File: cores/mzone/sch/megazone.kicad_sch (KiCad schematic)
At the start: 22 parts

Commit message: mzone core
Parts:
- removed B_DE9: 74LS32, symbol jt74:74LS32
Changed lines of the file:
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@@
 	(wire
 		(pts
-			(xy 68.58 135.89) (xy 76.2 135.89)
-		)
-		(stroke
-			(width 0)
-			(type default)
-		)
-	)
-	(wire
-		(pts
 			(xy 167.64 77.47) (xy 173.99 77.47)
 		)
@@
 	(wire
 		(pts
-			(xy 91.44 133.35) (xy 99.06 133.35)
-		)
-		(stroke
-			(width 0)
-			(type default)
-		)
-	)
-	(wire
-		(pts
 			(xy 127 218.44) (xy 127 220.98)
 		)
@@
 	(wire
 		(pts
-			(xy 68.58 130.81) (xy 76.2 130.81)
-		)
-		(stroke
-			(width 0)
-			(type default)
-		)
-	)
-	(wire
-		(pts
 			(xy 152.4 241.3) (xy 157.48 241.3)
 		)
@@
 		)
 	)
-	(label "~{MWRAMW}"
-		(at 91.44 133.35 0)
-		(fields_autoplaced yes)
-		(effects
-			(font
-				(size 1.27 1.27)
-			)
-			(justify left bottom)
-		)
-	)
-	(label "~{WRIT}"
-		(at 68.58 130.81 0)
-		(fields_autoplaced yes)
-		(effects
-			(font
-				(size 1.27 1.27)
-			)
-			(justify left bottom)
-		)
-	)
 	(label "~{AB}4"
 		(at 180.34 236.22 0)
@@
 		)
 	)
-	(label "~{MSHRAM}"
-		(at 68.58 135.89 0)
-		(fields_autoplaced yes)
-		(effects
-			(font
-				(size 1.27 1.27)
-			)
-			(justify left bottom)
-		)
-	)
 	(label "CLK1'"
 		(at 220.98 80.01 0)
@@
 					(unit 1)
 				)
-			)
-		)
-	)
-	(symbol
-		(lib_id "jt74:74LS32")
-		(at 83.82 133.35 0)
-		(unit 1)
-		(exclude_from_sim no)
-		(in_bom yes)
-		(on_board yes)
-		(dnp no)
-		(fields_autoplaced yes)
-		(property "Reference" "B_DE9"
-			(at 83.82 124.46 0)
-			(effects
-				(font
-					(size 1.27 1.27)
-				)
-			)
-		)
-		(property "Value" "74LS32"
-			(at 83.82 127 0)
-			(effects
-				(font
-					(size 1.27 1.27)
-				)
-			)
-		)
-		(property "Footprint" ""
-			(at 83.82 133.35 0)
-			(effects
-				(font
-					(size 1.27 1.27)
-				)
-				(hide yes)
-			)
-		)
-		(property "Datasheet" "http://www.ti.com/lit/gpn/sn74LS32"
-			(at 83.82 133.35 0)
-			(effects
-				(font
-					(size 1.27 1.27)
-				)
-				(hide yes)
-			)
-		)
-		(property "Description" ""
-			(at 83.82 133.35 0)
-			(effects
-				(font
-					(size 1.27 1.27)
-				)
-				(hide yes)
-			)
-		)
-		(pin "7"
-		)
-		(pin "14"
-		)
-		(pin "4"
-		)
-		(pin "1"
-		)
-		(pin "9"
-		)
-		(pin "10"
-		)
-		(pin "3"
-		)
-		(pin "2"
-		)
-		(pin "6"
-		)
-		(pin "8"
-		)
-		(pin "5"
-		)
-		(pin "13"
-		)
-		(pin "11"
-		)
-		(pin "12"
-		)
-		(instances
-			(project "megazone"
-				(path "/b3e039a8-74b0-4cb4-b612-5df1f0b42747"
-					(reference "B_DE9")
-					(unit 1)
-				)

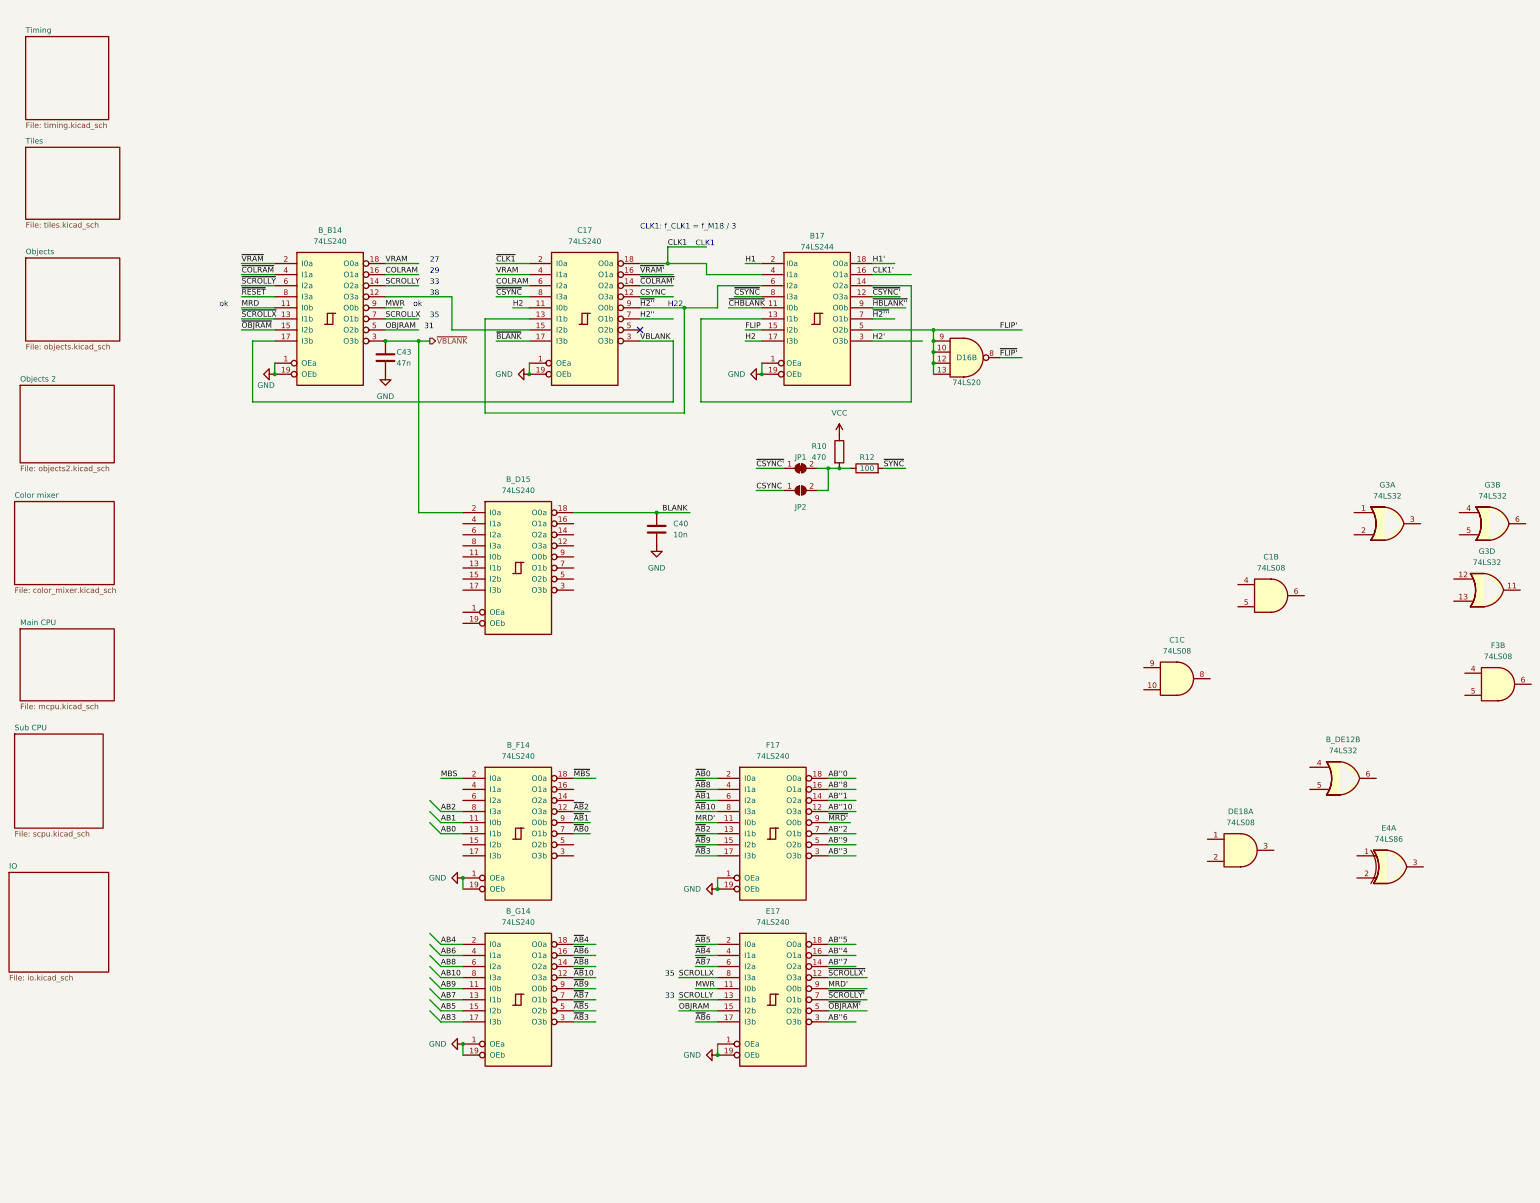
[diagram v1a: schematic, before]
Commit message: mzone core
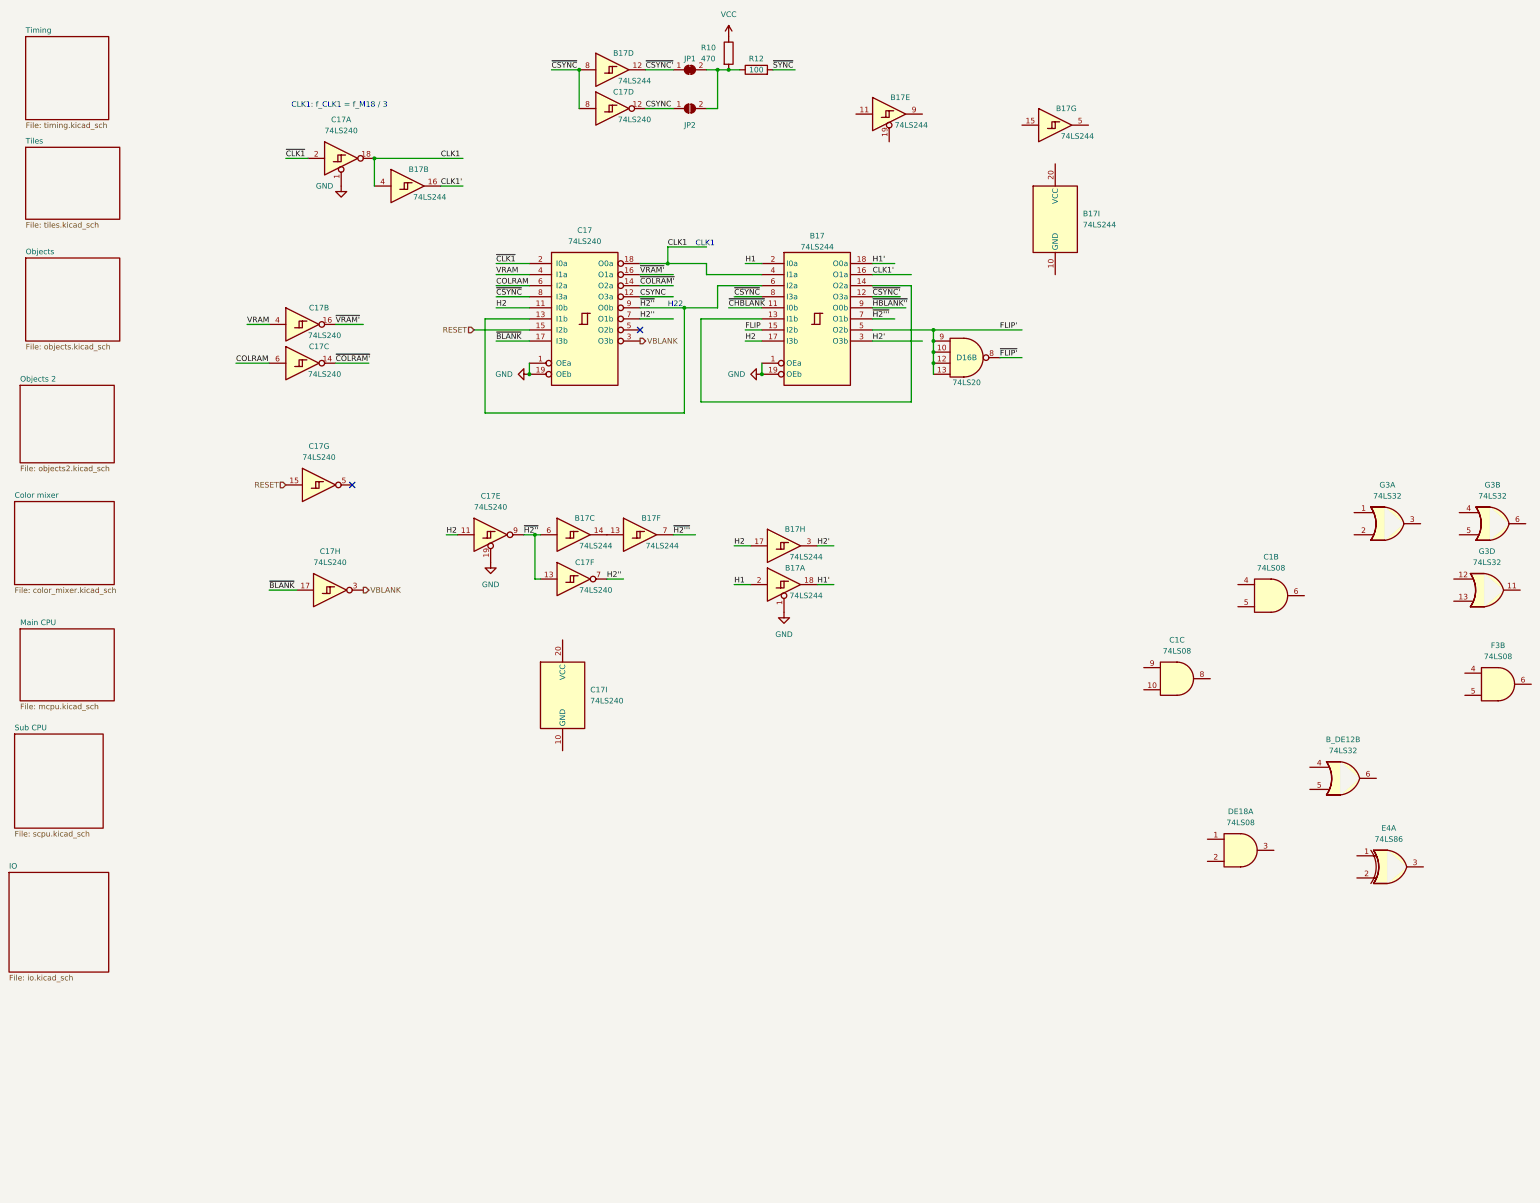
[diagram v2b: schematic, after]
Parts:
- removed B_B14, B_D15, B_F14, B_G14, E17, F17: 74LS240, symbol jt74:74LS240
- removed C40: 10n, symbol Device:C
- removed C43: 47n, symbol Device:C
- added unit 3 of B17
- added unit 2 of B17
- added unit 4 of B17
- added unit 8 of B17
- added unit 6 of B17
- added unit 9 of B17
- added unit 5 of B17
- added unit 7 of B17
- added C17: 74LS240, symbol 74xx:74LS240_Split
- added unit 7 of C17
- added unit 9 of C17
- added unit 2 of C17
- added unit 8 of C17
- added unit 5 of C17
- added unit 4 of C17
- added unit 3 of C17
- added unit 6 of C17
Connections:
- net CLK1: now also B17.4, C17.18
- net CLK1': now also B17.16
- net COLRAM: now also C17.6
- net CSYNC: now also C17.12
- net GND: now also B17.1, C17.1, C17.19
- net H1: now also B17.2
- net H1': now also B17.18
- net H2: now also B17.17, C17.11
- net H2': now also B17.3
- net H2'': now also C17.7
- net VBLANK: now also C17.3
- net VRAM: now also C17.4
- net ~{BLANK}: now also C17.17
- net ~{CLK1}: now also C17.2
- net ~{COLRAM'}: now also C17.14
- net ~{CSYNC'}: now also B17.12
- net ~{CSYNC}: now also B17.8, C17.8
- net ~{H2'''}: now also B17.7
- net ~{H2''}: now also B17.6, C17.13, C17.9
- net ~{VRAM'}: now also C17.16
- net RESET: now reaches C17.15 (I2b)
- net RESET: now also C17.15
- new net: B17.13, B17.14
- no-connect marks 1 -> 2
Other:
- note removed: "27"
- note removed: "29"
- note removed: "31"
- note removed: "33"
- note removed: "35"
- note removed: "38"
- note removed: "ok"
- moved on the sheet: JP1, JP2, R10, R12

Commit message: mzone core
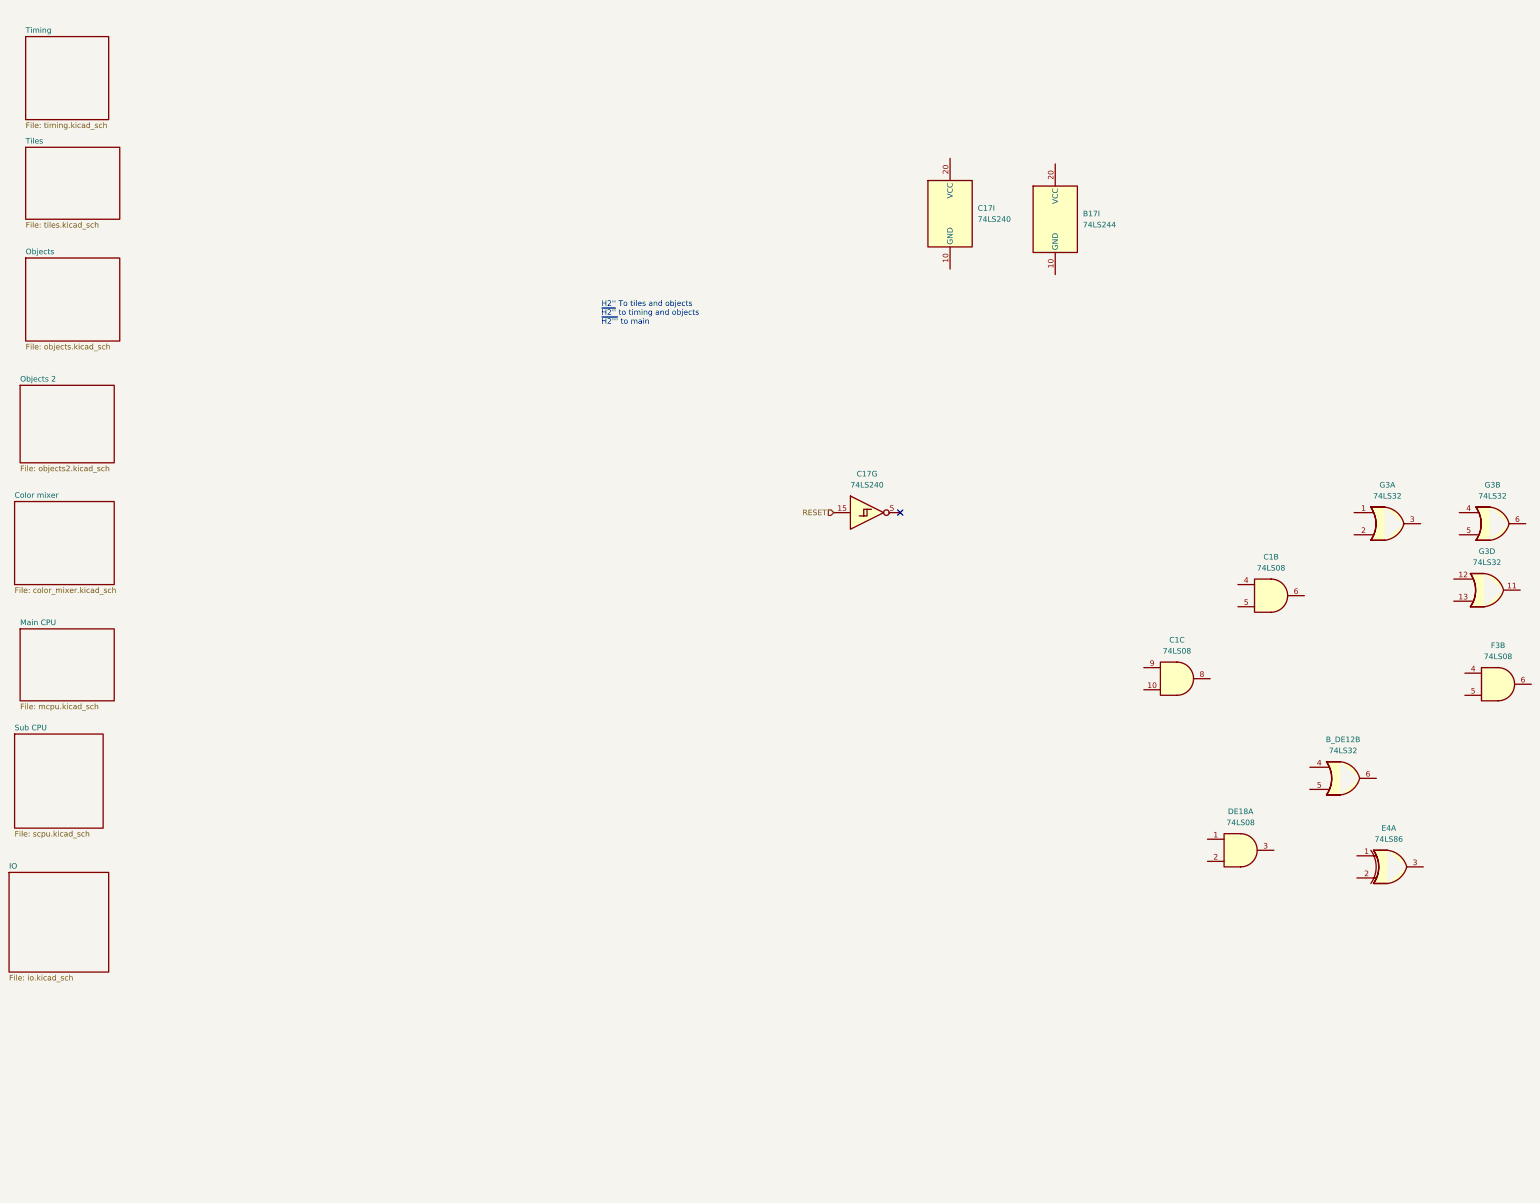
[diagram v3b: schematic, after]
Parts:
- removed unit 3 of B17
- removed unit 2 of B17
- removed unit 1 of B17 (x2)
- removed unit 4 of B17
- removed unit 8 of B17
- removed unit 6 of B17
- removed unit 5 of B17
- removed unit 7 of B17
- removed unit 1 of C17 (x2)
- removed unit 2 of C17
- removed unit 8 of C17
- removed unit 5 of C17
- removed unit 4 of C17
- removed unit 3 of C17
- removed unit 6 of C17
- removed D16: 74LS20, symbol jt74:74LS20
- removed JP1: SolderJumper_2_Bridged, symbol Jumper:SolderJumper_2_Bridged
- removed JP2: SolderJumper_2_Open, symbol Jumper:SolderJumper_2_Open
- removed R10: 470, symbol Device:R
- removed R12: 100, symbol Device:R
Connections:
- no-connect marks 2 -> 1
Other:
- note added: "H2'' To tiles and objects ~{H2''} to timing and objects ~{H2'''} to main"
- note removed: "CLK1"
- note removed: "CLK1: f_CLK1 = f_M18 / 3"
- note removed: "H22"
- moved on the sheet: C17G, C17I

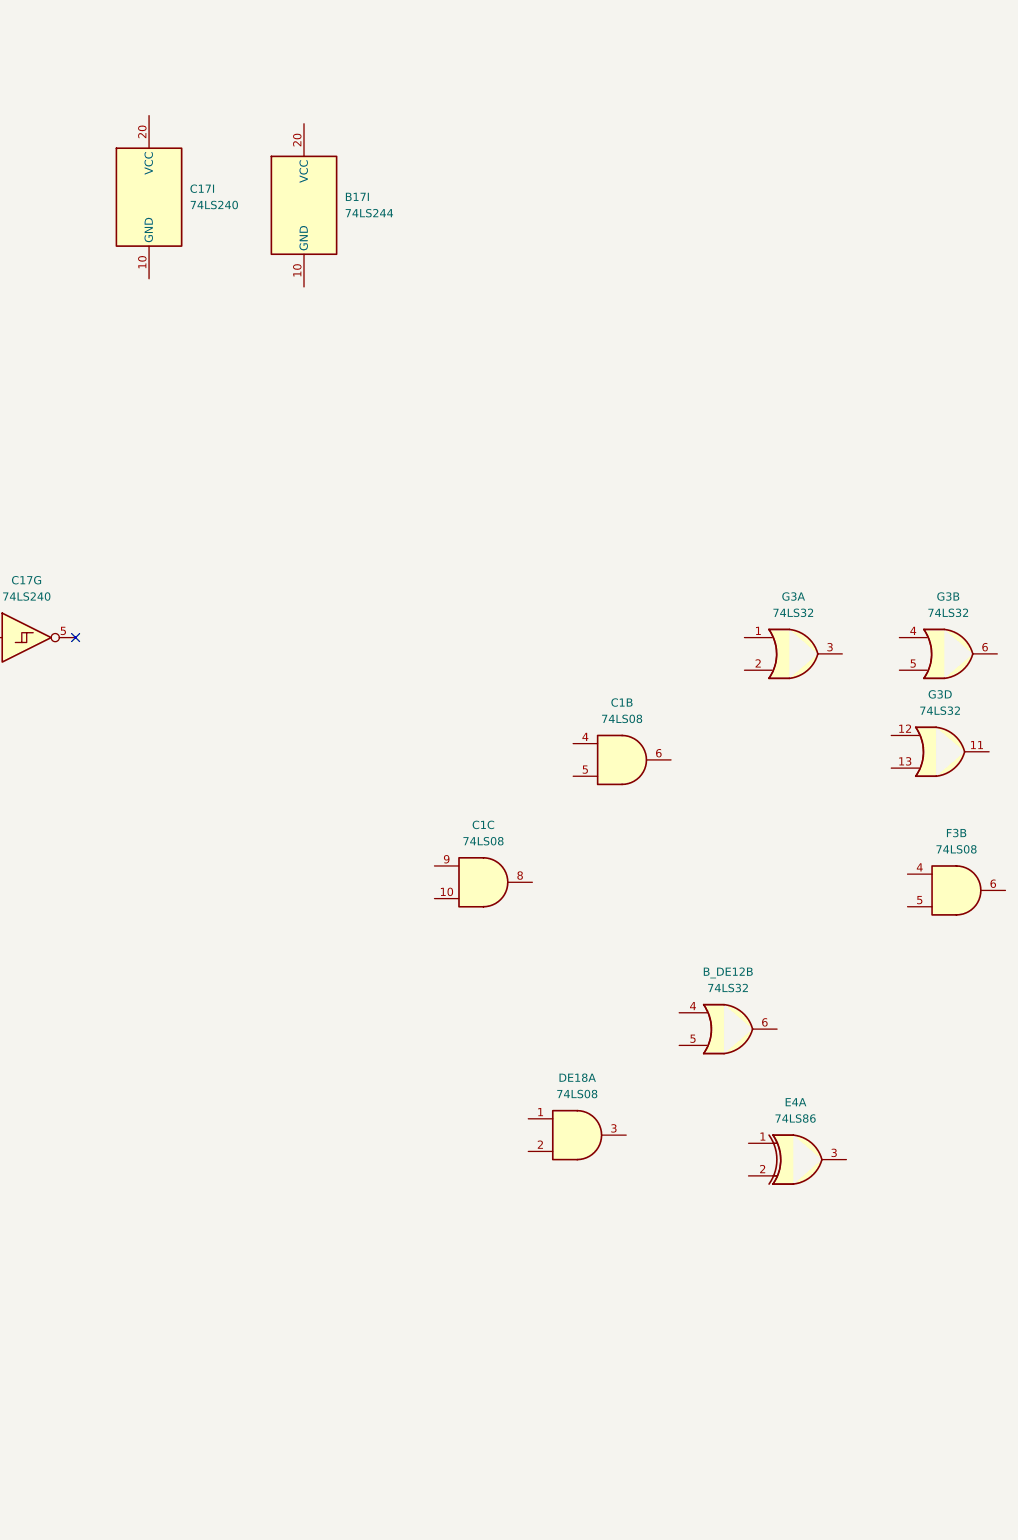
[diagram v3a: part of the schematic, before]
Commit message: mzone core
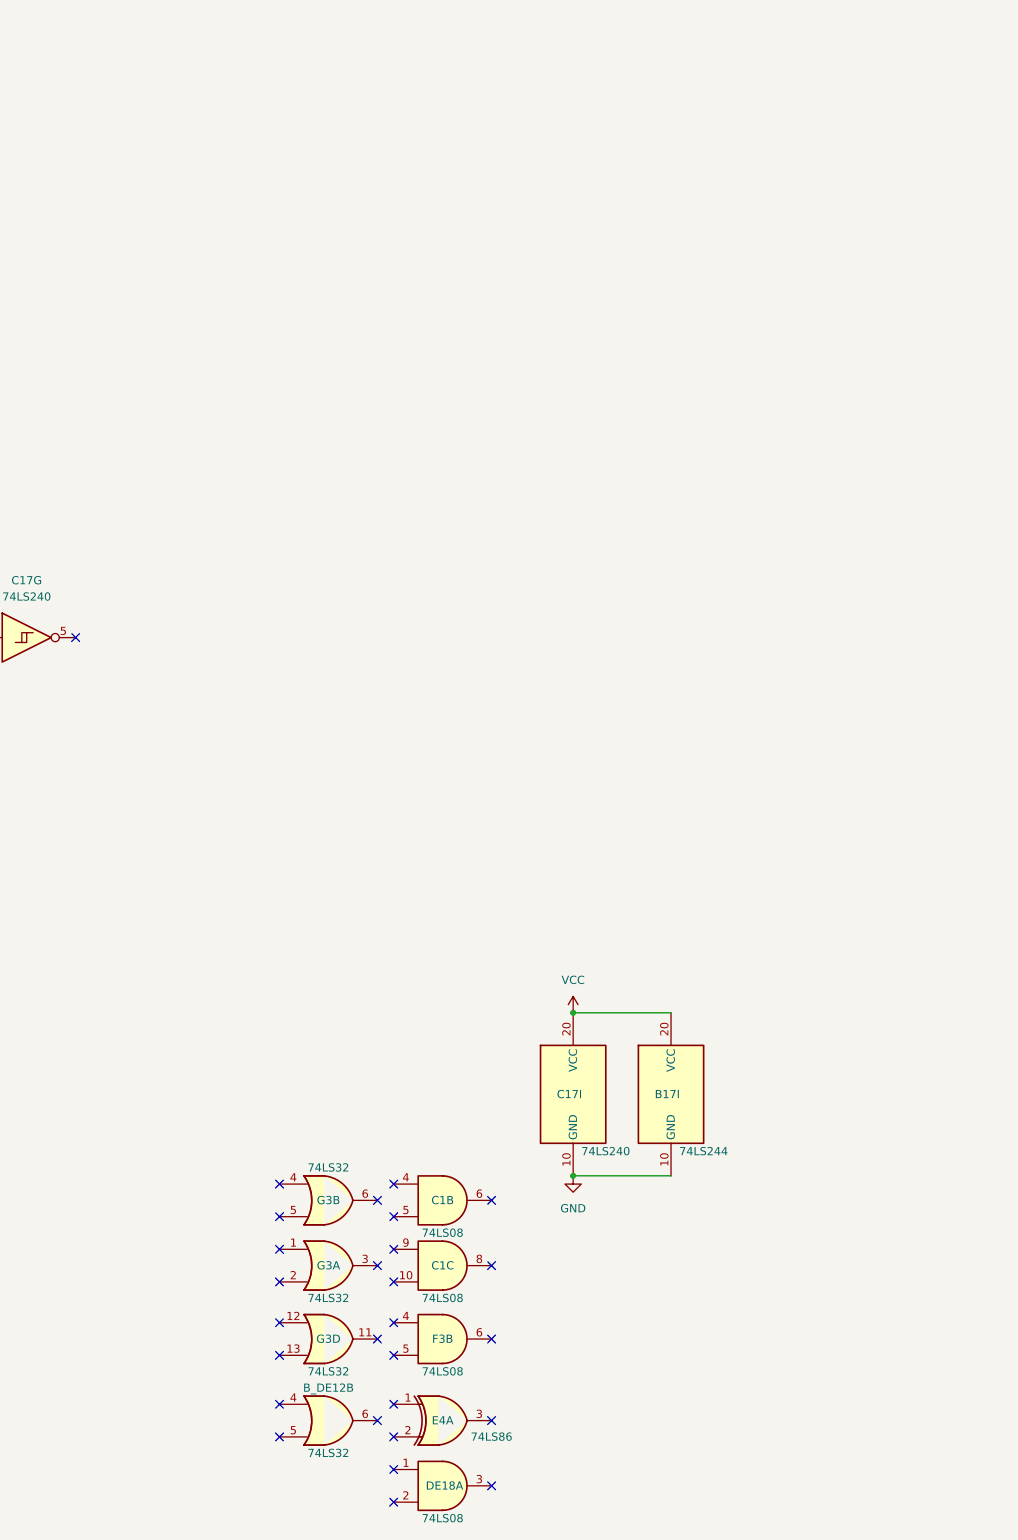
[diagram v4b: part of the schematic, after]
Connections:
- net GND: now reaches C17.10 (GND)
- net GND: now also B17.10 (GND)
- net VCC: now reaches C17.20 (VCC)
- net VCC: now also B17.20 (VCC)
- no-connect marks 1 -> 28
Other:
- moved on the sheet: B17I, B_DE12B, C17I, C1B, C1C, DE18A, E4A, F3B, G3A, G3B, G3D
